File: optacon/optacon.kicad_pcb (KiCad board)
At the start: 2 copper layers, 31.7 x 90.2 mm, 35 parts, among them J1 Conn_01x12, U1 HV528, U2 HV528, U3 DRV2665

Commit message: pcb + stencils ordered from pcbgogo
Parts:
- moved TP10 4.20 mm to (111.5, 44.5)
- moved TP11 4.20 mm to (111.5, 48.8)
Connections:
- C3 pad 1: Net-(C3-Pad1) -> /EN
- R6 pad 2: Net-(C3-Pad1) -> /EN
- TP11 pad 1: /REG -> /EN
- U3 pad 20: Net-(C3-Pad1) -> /EN
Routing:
- net /EN: track 0.00 -> 14.2 mm, vias 0 -> 2
- net /REG: track 15.0 -> 7.84 mm, vias 3 -> 2
- net Net-(C3-Pad1): track 5.63 -> 0.00 mm
- net /SCL: track 20.7 -> 21.2 mm

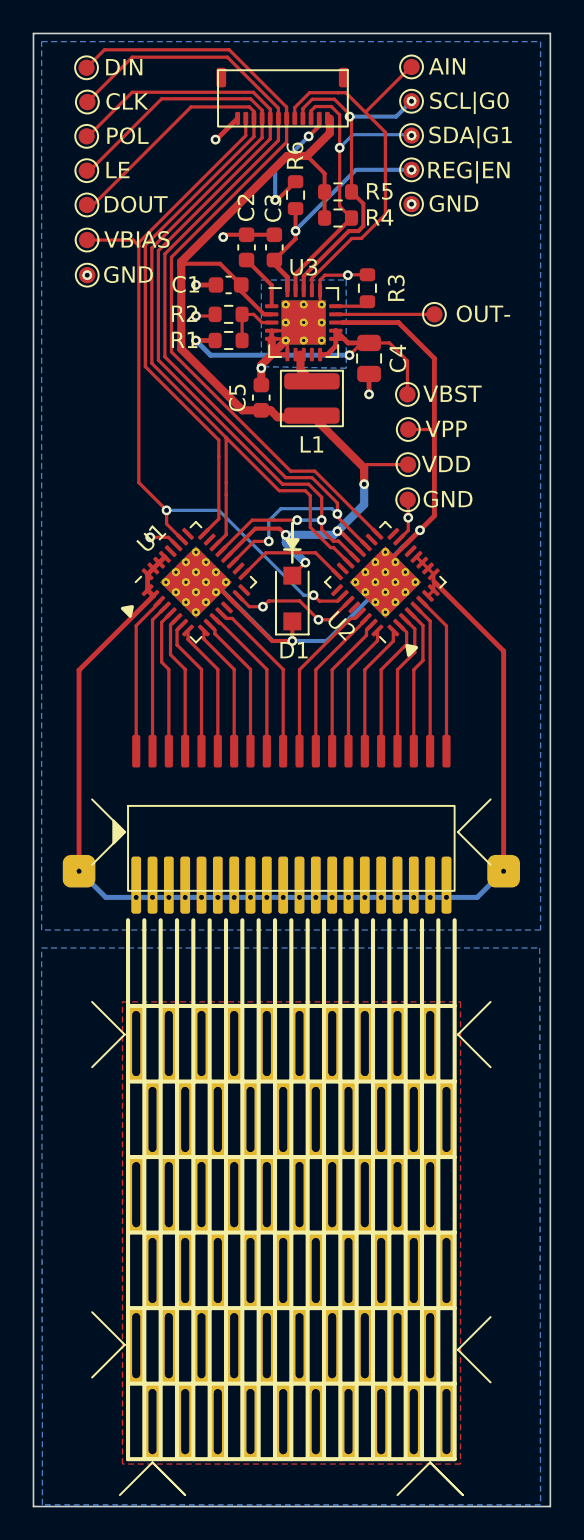
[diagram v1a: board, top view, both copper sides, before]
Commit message: remove VBIAS, EN, REG rename & reorder nets for i2c, spi add IN- next to IN+ (AIN) add SMD FPC connector for piezo use BP instead of HVOUTs for piezo_common
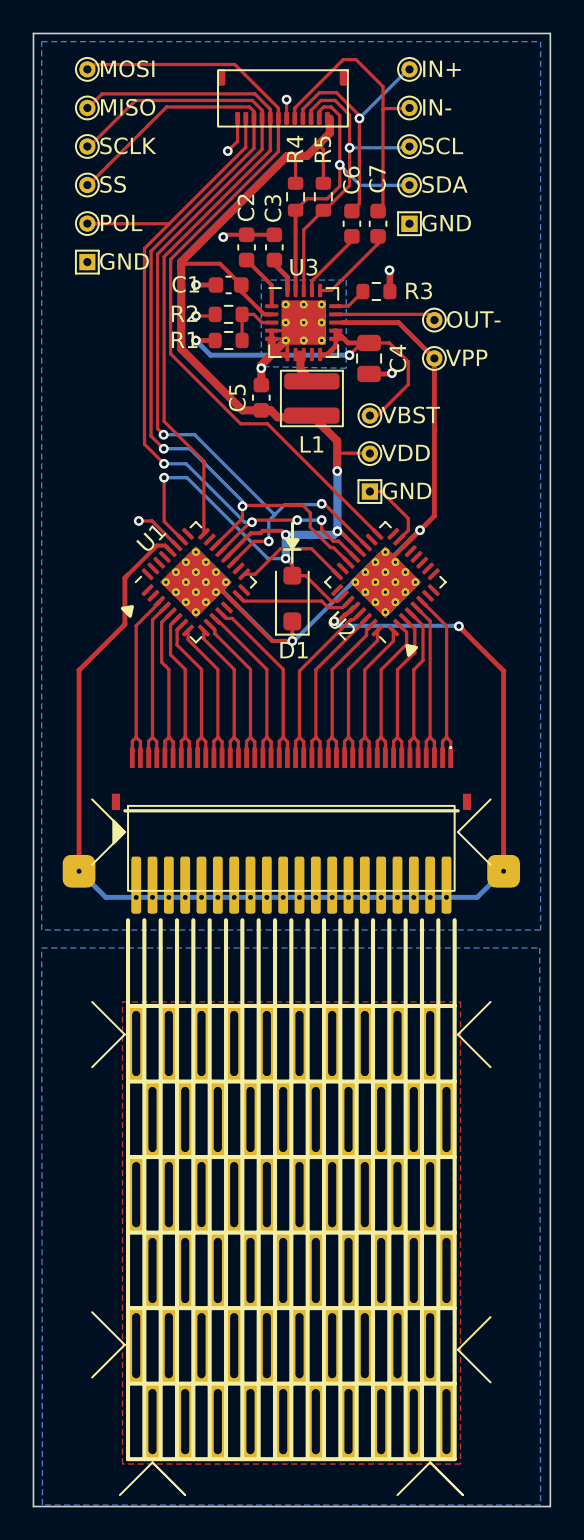
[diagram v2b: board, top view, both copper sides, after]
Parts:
- removed R6: DNP, Resistor_SMD:R_0603_1608Metric
- removed TP11, TP15: TestPoint, TestPoint:TestPoint_Pad_D1.0mm
- added C6: 1 µF, Capacitor_SMD:C_0603_1608Metric, F.Cu at (107.8, 52.0)
- added C7: 1 µF, Capacitor_SMD:C_0603_1608Metric, F.Cu at (109.5, 52.0)
- added IN-: TestPoint, TestPoint:TestPoint_THTPad_D1.0mm_Drill0.5mm, F.Cu at (111.4, 45.0)
- added J2: Conn_01x40_Socket, microchip_hv:FH34SRJ-40S-0.5SH, F.Cu at (104.2, 86.5)
- GND (x3): renamed from TP2; footprint TestPoint:TestPoint_Pad_D1.0mm -> TestPoint:TestPoint_THTPad_1.0x1.0mm_Drill0.5mm
- IN+: renamed from TP6; footprint TestPoint:TestPoint_Pad_D1.0mm -> TestPoint:TestPoint_THTPad_D1.0mm_Drill0.5mm
- MISO: renamed from TP8; footprint TestPoint:TestPoint_Pad_D1.0mm -> TestPoint:TestPoint_THTPad_D1.0mm_Drill0.5mm
- MOSI: renamed from TP7; footprint TestPoint:TestPoint_Pad_D1.0mm -> TestPoint:TestPoint_THTPad_D1.0mm_Drill0.5mm
- OUT-: renamed from TP5; footprint TestPoint:TestPoint_Pad_D1.0mm -> TestPoint:TestPoint_THTPad_D1.0mm_Drill0.5mm
- POL: renamed from TP13; footprint TestPoint:TestPoint_Pad_D1.0mm -> TestPoint:TestPoint_THTPad_D1.0mm_Drill0.5mm
- SCL: renamed from TP10; footprint TestPoint:TestPoint_Pad_D1.0mm -> TestPoint:TestPoint_THTPad_D1.0mm_Drill0.5mm
- SCLK: renamed from TP12; footprint TestPoint:TestPoint_Pad_D1.0mm -> TestPoint:TestPoint_THTPad_D1.0mm_Drill0.5mm
- SDA: renamed from TP9; footprint TestPoint:TestPoint_Pad_D1.0mm -> TestPoint:TestPoint_THTPad_D1.0mm_Drill0.5mm
- SS: renamed from TP14; footprint TestPoint:TestPoint_Pad_D1.0mm -> TestPoint:TestPoint_THTPad_D1.0mm_Drill0.5mm
- U1, U2: value HV528 -> HV509
- VBST: renamed from TP4; footprint TestPoint:TestPoint_Pad_D1.0mm -> TestPoint:TestPoint_THTPad_D1.0mm_Drill0.5mm
- VDD: renamed from TP1; footprint TestPoint:TestPoint_Pad_D1.0mm -> TestPoint:TestPoint_THTPad_D1.0mm_Drill0.5mm
- VPP: renamed from TP3; footprint TestPoint:TestPoint_Pad_D1.0mm -> TestPoint:TestPoint_THTPad_D1.0mm_Drill0.5mm
- moved MISO 5.94 mm to (91.7, 45.0)
- moved POL 5.34 mm to (91.7, 52.0)
- moved VPP 4.63 mm to (112.9, 60.3)
- moved SDA 3.04 mm to (111.4, 49.7)
- moved R4 2.91 mm to (104.4, 50.4), turned to -90 degrees
- moved SCL 2.78 mm to (111.4, 47.3)
- moved SCLK 2.72 mm to (91.7, 47.3)
- moved VBST 2.64 mm to (109.0, 63.8)
- moved VDD 2.43 mm to (109.0, 66.1)
- moved GND 2.37 mm to (109.0, 68.5)
- moved GND 1.21 mm to (111.4, 52.0)
- moved R5 0.95 mm to (106.1, 50.4), turned to 90 degrees
- moved SS 0.88 mm to (91.7, 49.7)
- moved GND 0.80 mm to (91.7, 54.4)
- moved R3 0.59 mm to (109.3, 56.2), turned to 0 degrees
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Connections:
- net /EN renamed Net-(U3-REG)
- IN+ pad 1: /AIN -> /IN+
- J1 pad 10: /SDA -> /SCL
- J1 pad 11: /REG -> /SDA
- J1 pad 2: /VBIAS -> /POL
- J1 pad 3: /DOUT -> /SS
- J1 pad 4: /LE -> /SCLK
- J1 pad 5: /POL -> /MISO
- J1 pad 6: /CLK -> /MOSI
- J1 pad 7: /DIN -> GND
- J1 pad 8: /AIN -> /IN-
- J1 pad 9: /SCL -> /IN+
- MISO pad 1: /DOUT -> /MISO
- MOSI pad 1: /DIN -> /MOSI
- SCLK pad 1: /CLK -> /SCLK
- SS pad 1: /LE -> /SS
- U1 pad 1: /PZT_Common -> unconnected-(U1-HVout12-Pad1)
- U1 pad 19: /CLK -> /SCLK
- U1 pad 2: /PZT_Common -> unconnected-(U1-HVout11-Pad2)
- U1 pad 22: /LE -> /SS
- U1 pad 24: /DOUT -> /MISO
- U1 pad 26: /VBIAS -> /VDD
- U1 pad 28: unconnected-(U1-Pad28) -> /PZT_Common
- U1 pad 29: /PZT_Common -> unconnected-(U1-HVout16-Pad29)
- U1 pad 30: /PZT_Common -> unconnected-(U1-HVout15-Pad30)
- U1 pad 31: /PZT_Common -> unconnected-(U1-HVout14-Pad31)
- U1 pad 32: /PZT_Common -> unconnected-(U1-HVout13-Pad32)
- U2 pad 10: /PZT_Common -> unconnected-(U2-HVout3-Pad10)
- U2 pad 11: /PZT_Common -> unconnected-(U2-HVout2-Pad11)
- U2 pad 12: /PZT_Common -> unconnected-(U2-HVout1-Pad12)
- U2 pad 17: /DIN -> /MOSI
- U2 pad 19: /CLK -> /SCLK
- U2 pad 22: /LE -> /SS
- U2 pad 26: /VBIAS -> /VDD
- U2 pad 28: unconnected-(U2-Pad28) -> /PZT_Common
- U2 pad 7: /PZT_Common -> unconnected-(U2-HVout6-Pad7)
- U2 pad 8: /PZT_Common -> unconnected-(U2-HVout5-Pad8)
- U2 pad 9: /PZT_Common -> unconnected-(U2-HVout4-Pad9)
- U3 pad 16: GND -> Net-(U3-IN-)
- U3 pad 17: /AIN -> Net-(U3-IN+)
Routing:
- net /CLK: track 58.5 -> 0.00 mm, vias 2 -> 0
- net /LE: track 56.2 -> 0.00 mm
- net /SCLK: track 0.00 -> 55.1 mm, vias 0 -> 3
- net /SS: track 0.00 -> 53.9 mm, vias 0 -> 2
- net /DIN: track 49.3 -> 0.00 mm
- net /MOSI: track 0.00 -> 47.9 mm
- net /VBIAS: track 46.1 -> 0.00 mm, vias 2 -> 0
- net /DOUT: track 43.6 -> 0.00 mm
- net /MISO: track 0.00 -> 41.7 mm
- net /AIN: track 23.4 -> 0.00 mm
- net /IN-: track 0.00 -> 17.3 mm
- net /IN+: track 0.00 -> 15.3 mm, vias 0 -> 1
- net /VDD: track 64.5 -> 79.2 mm, vias 4 -> 5
- net Net-(U3-REG): track 14.2 -> 1.94 mm, vias 2 -> 0
- net /POL: track 56.0 -> 46.3 mm, vias 2 -> 4
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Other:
- board text added: "piezo driver board rev 3"
- board text removed: "piezo driver board rev 2.1"

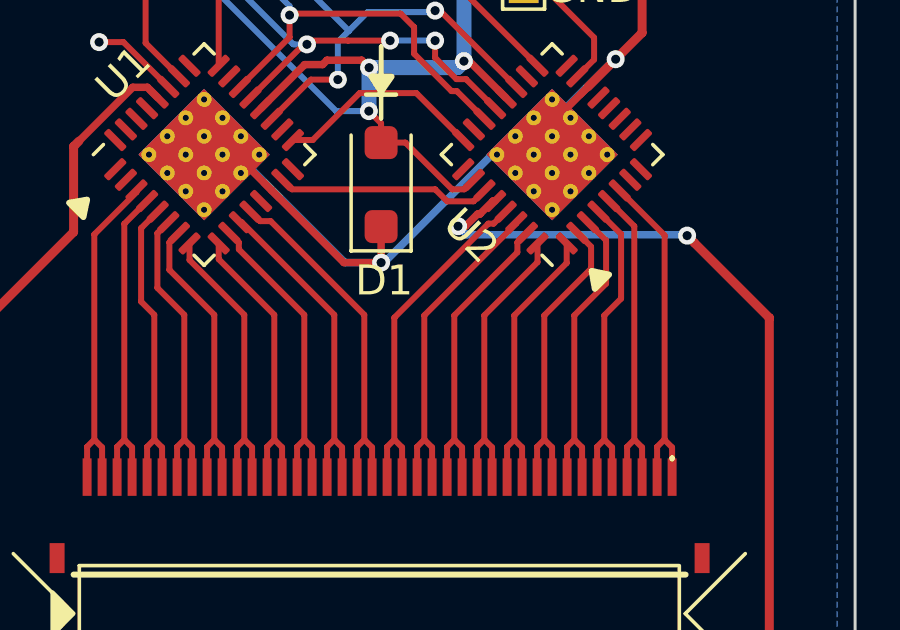
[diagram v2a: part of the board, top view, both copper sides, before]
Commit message: J2 (mounting) pads no paste
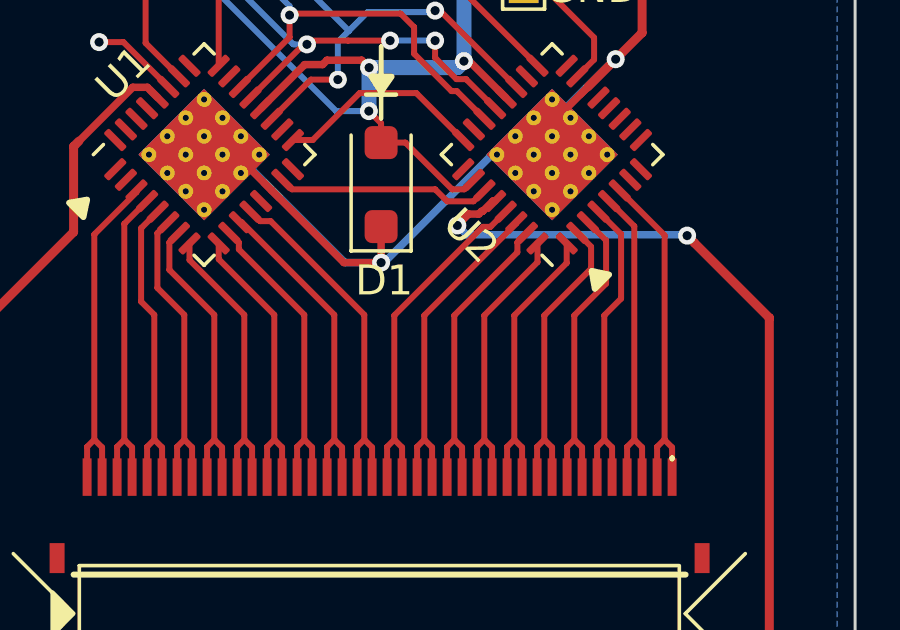
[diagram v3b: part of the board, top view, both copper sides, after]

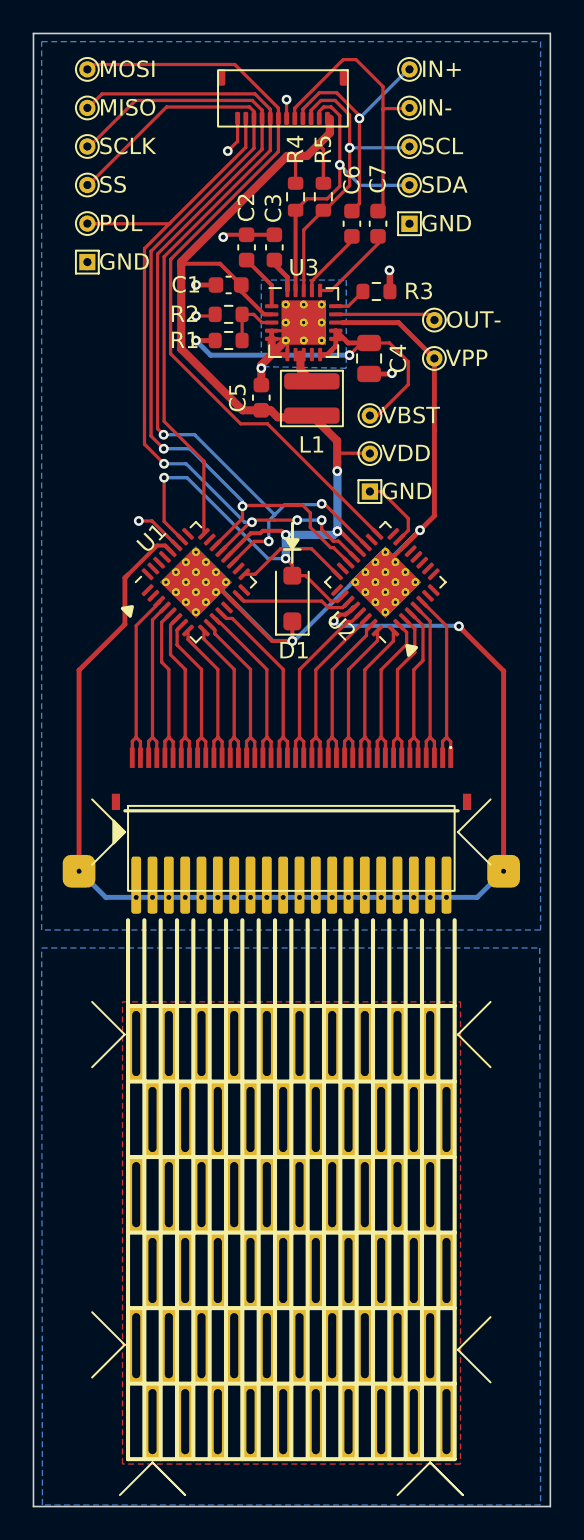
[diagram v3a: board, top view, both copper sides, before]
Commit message: separate VIN and VDD
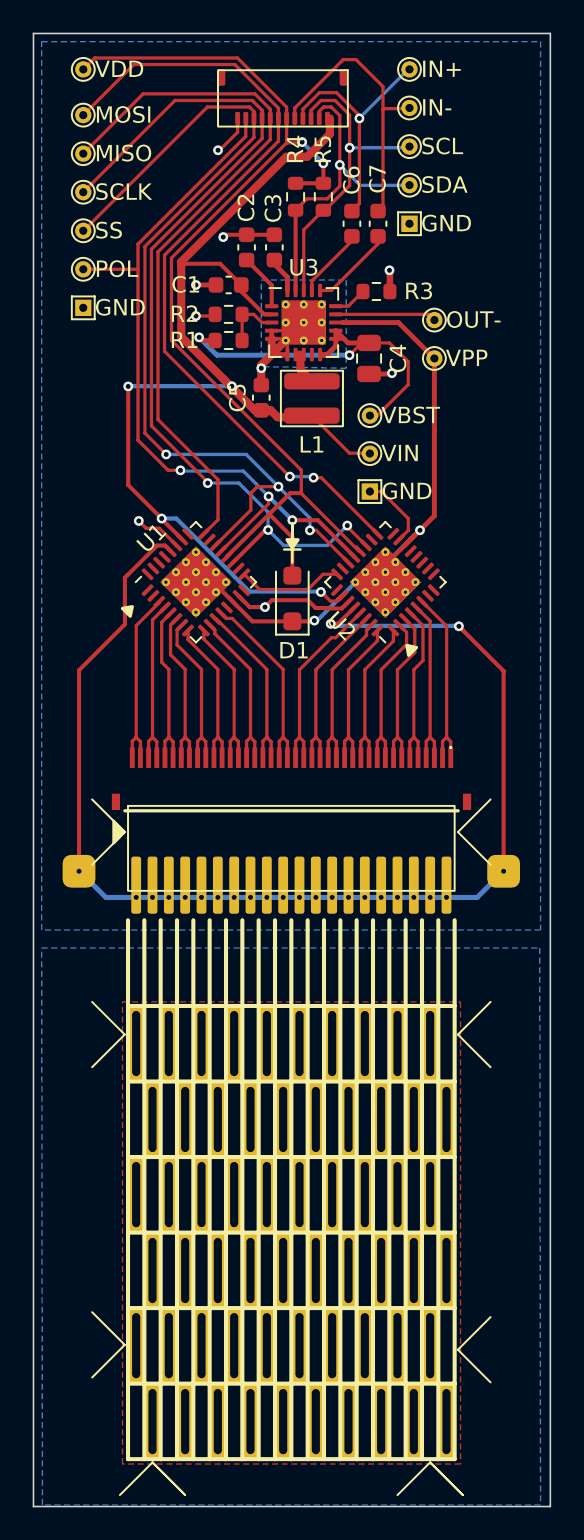
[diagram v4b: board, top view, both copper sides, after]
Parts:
- added TP15: VDD, TestPoint:TestPoint_THTPad_D1.0mm_Drill0.5mm, F.Cu at (109.0, 66.1)
- TP1: renamed from VDD; value TestPoint -> VDD
- U1, U2: value HV509 -> HV528
- moved TP1 29.4 mm to (91.4, 42.6)
- moved TP13 2.81 mm to (91.4, 54.8)
- moved TP2 2.81 mm to (91.4, 57.2)
- moved TP12 2.81 mm to (91.4, 50.1)
- moved TP14 2.81 mm to (91.4, 52.5)
- moved TP8 2.81 mm to (91.4, 45.4)
- moved TP9 2.81 mm to (91.4, 47.8)
- renumbered SDA to TP10, SCL to TP11, SCLK to TP12, POL to TP13, SS to TP14, GND to TP2, VPP to TP3, VBST to TP4, OUT- to TP5, IN+ to TP6, IN- to TP7, MOSI to TP8, MISO to TP9
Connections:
- C1 pad 1: /VDD -> /VIN
- C5 pad 1: /VDD -> /VIN
- J1 pad 12: /VDD -> /VIN
- J1 pad 7: GND -> /VDD
- L1 pad 2: /VDD -> /VIN
- U1 pad 26: /VDD -> /VIN
- U2 pad 26: /VDD -> /VIN
- U3 pad 2: /VDD -> /VIN
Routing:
- net /VIN: track 0.00 -> 70.7 mm, vias 0 -> 4
- net /VDD: track 79.2 -> 65.2 mm, vias 5 -> 2
- net /VPP: track 51.2 -> 41.6 mm
- net /SS: track 53.9 -> 58.3 mm, vias 2 -> 3
- net /MISO: track 41.7 -> 44.1 mm
- net /MOSI: track 47.9 -> 49.8 mm, vias 0 -> 2
- net /SCLK: track 55.1 -> 56.6 mm
- net GND: track 36.3 -> 35.4 mm
- net Net-(U1-DIN): track 6.97 -> 6.45 mm
- net /POL: track 46.3 -> 46.5 mm, vias 4 -> 3

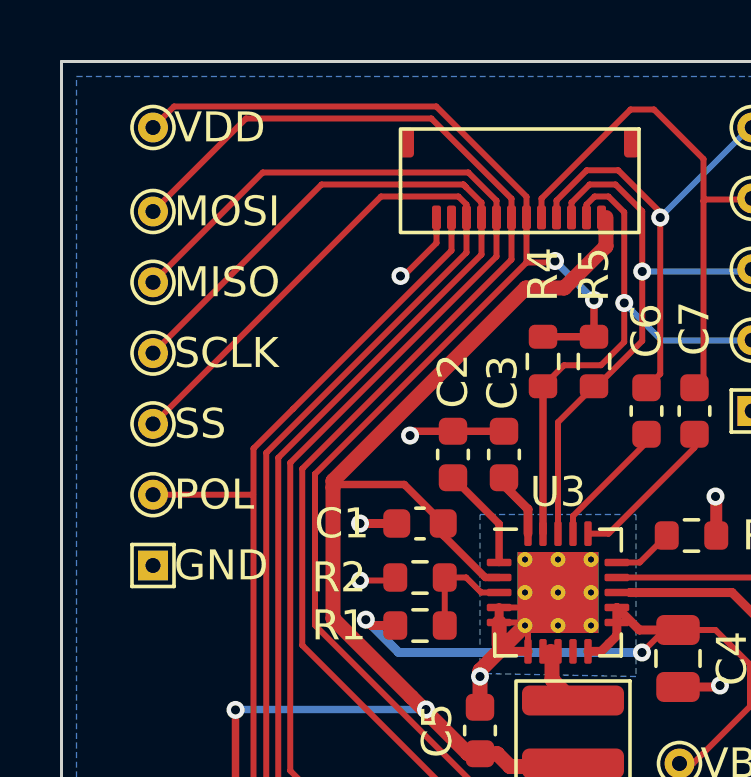
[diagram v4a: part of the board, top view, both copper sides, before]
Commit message: realign test points
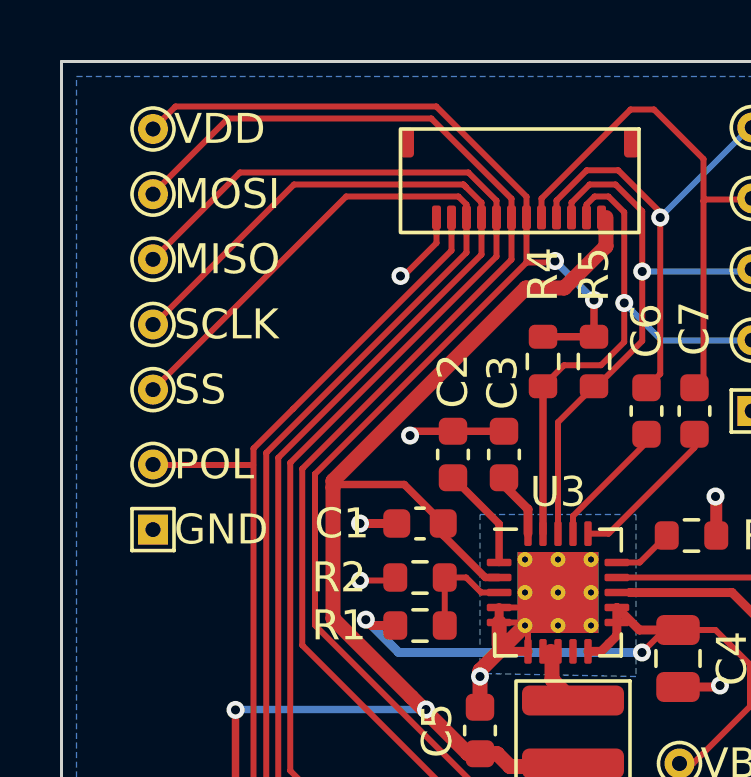
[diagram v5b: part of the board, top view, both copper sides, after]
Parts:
- moved TP2 1.20 mm to (91.4, 56.0)
- moved TP14 1.14 mm to (91.4, 51.3)
- moved TP13 1.01 mm to (91.4, 53.8)
- moved TP12 0.95 mm to (91.4, 49.2)
- moved TP9 0.77 mm to (91.4, 47.0)
- moved TP8 0.58 mm to (91.4, 44.8)
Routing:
- net /SS: track 58.3 -> 57.8 mm
